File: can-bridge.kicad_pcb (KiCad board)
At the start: 2 copper layers, 59.5 x 54 mm, 14 parts, among them J102 CAN1, SW101 78RB02ST, SW102 Reset, U102 MCP2551-I-SN, U104 TXB0104PW

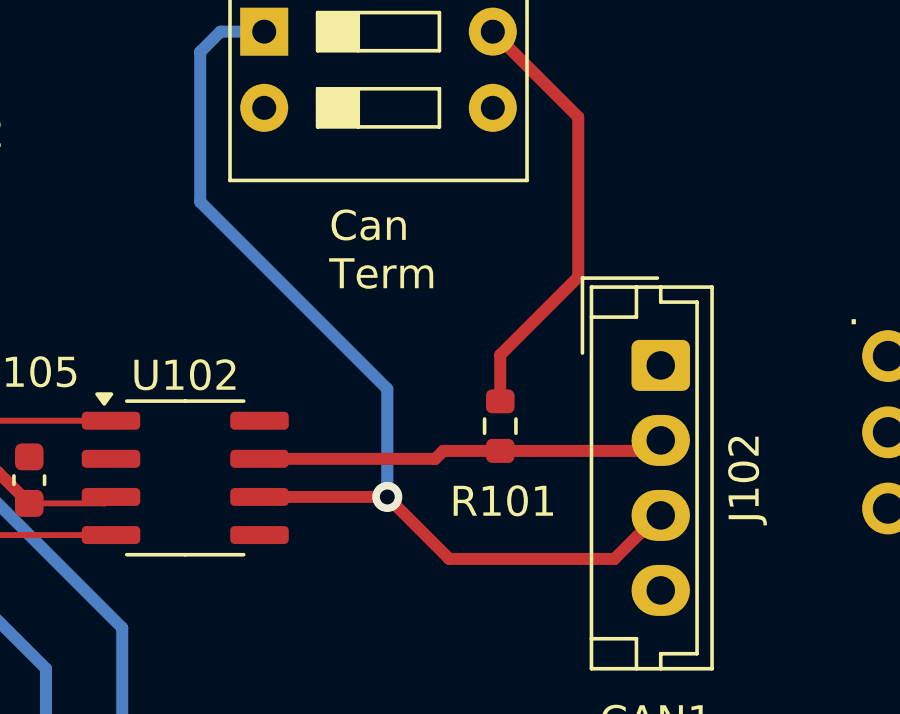
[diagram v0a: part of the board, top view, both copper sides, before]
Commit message: Added README.md and image of prototype
Changed R101 resistor to 1206 footprint
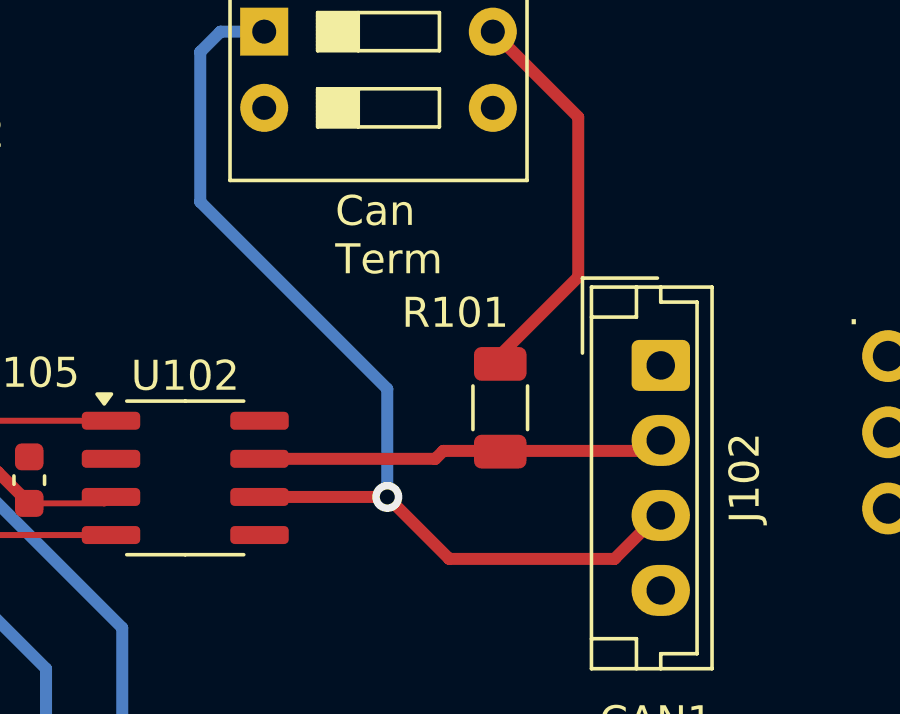
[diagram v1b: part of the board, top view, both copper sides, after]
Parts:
- R101: footprint Resistor_SMD:R_0603_1608Metric -> Resistor_SMD:R_1206_3216Metric
- moved R101 0.61 mm to (162.5, 98.5)
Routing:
- net Net-(R101-Pad1): track 14.6 -> 13.0 mm
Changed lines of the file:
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@@
 		)
 	)
-	(footprint "Resistor_SMD:R_0603_1608Metric"
+	(footprint "Resistor_SMD:R_1206_3216Metric"
 		(layer "F.Cu")
-		(at 162.5 99.075 -90)
-		(descr "Resistor SMD 0603 (1608 Metric), square (rectangular) end terminal, IPC_7351 nominal, (Body size source: IPC-SM-782 page 72, https://www.pcb-3d.com/wordpress/wp-content/uploads/ipc-sm-782a_amendment_1_and_2.pdf), generated with kicad-footprint-generator")
+		(at 162.5 98.4625 -90)
+		(descr "Resistor SMD 1206 (3216 Metric), square (rectangular) end terminal, IPC_7351 nominal, (Body size source: IPC-SM-782 page 72, https://www.pcb-3d.com/wordpress/wp-content/uploads/ipc-sm-782a_amendment_1_and_2.pdf), generated with kicad-footprint-generator")
 		(tags "resistor")
 		(property "Reference" "R101"
-			(at 2.525 -0.1 180)
+			(at -3.1625 1.5 0)
 			(layer "F.SilkS")
 			(effects
@@
 		)
 		(property "Value" "120"
-			(at 0 1.43 90)
+			(at 0 1.82 -90)
 			(layer "F.Fab")
 			(effects
@@
 			)
 		)
-		(property "Footprint" "Resistor_SMD:R_0603_1608Metric"
+		(property "Footprint" "Resistor_SMD:R_1206_3216Metric"
 			(at 0 0 -90)
 			(unlocked yes)
@@
 		(attr smd)
 		(fp_line
-			(start -0.237258 0.5225)
-			(end 0.237258 0.5225)
+			(start -0.727064 0.91)
+			(end 0.727064 0.91)
 			(stroke
 				(width 0.12)
@@
 		)
 		(fp_line
-			(start -0.237258 -0.5225)
-			(end 0.237258 -0.5225)
+			(start -0.727064 -0.91)
+			(end 0.727064 -0.91)
 			(stroke
 				(width 0.12)
@@
 		)
 		(fp_line
-			(start -1.48 0.73)
-			(end -1.48 -0.73)
+			(start -2.28 1.12)
+			(end -2.28 -1.12)
 			(stroke
 				(width 0.05)
@@
 		)
 		(fp_line
-			(start 1.48 0.73)
-			(end -1.48 0.73)
+			(start 2.28 1.12)
+			(end -2.28 1.12)
 			(stroke
 				(width 0.05)
@@
 		)
 		(fp_line
-			(start -1.48 -0.73)
-			(end 1.48 -0.73)
+			(start -2.28 -1.12)
+			(end 2.28 -1.12)
 			(stroke
 				(width 0.05)
@@
 		)
 		(fp_line
-			(start 1.48 -0.73)
-			(end 1.48 0.73)
+			(start 2.28 -1.12)
+			(end 2.28 1.12)
 			(stroke
 				(width 0.05)
@@
 		)
 		(fp_line
-			(start -0.8 0.4125)
-			(end -0.8 -0.4125)
+			(start -1.6 0.8)
+			(end -1.6 -0.8)
 			(stroke
 				(width 0.1)
@@
 		)
 		(fp_line
-			(start 0.8 0.4125)
-			(end -0.8 0.4125)
+			(start 1.6 0.8)
+			(end -1.6 0.8)
 			(stroke
 				(width 0.1)
@@
 		)
 		(fp_line
-			(start -0.8 -0.4125)
-			(end 0.8 -0.4125)
+			(start -1.6 -0.8)
+			(end 1.6 -0.8)
 			(stroke
 				(width 0.1)
@@
 		)
 		(fp_line
-			(start 0.8 -0.4125)
-			(end 0.8 0.4125)
+			(start 1.6 -0.8)
+			(end 1.6 0.8)
 			(stroke
 				(width 0.1)
@@
 		)
 		(fp_text user "${REFERENCE}"
-			(at 0 0 90)
+			(at 0 0 -90)
 			(layer "F.Fab")
 			(effects
 				(font
-					(size 0.4 0.4)
-					(thickness 0.06)
+					(size 0.8 0.8)
+					(thickness 0.12)
 				)
 			)
 		)
 		(pad "1" smd roundrect
-			(at -0.825 0 270)
-			(size 0.8 0.95)
+			(at -1.4625 0 270)
+			(size 1.125 1.75)
 			(layers "F.Cu" "F.Paste" "F.Mask")
-			(roundrect_rratio 0.25)
+			(roundrect_rratio 0.222222)
 			(net 51 "Net-(R101-Pad1)")
 			(pintype "passive")
 		)
 		(pad "2" smd roundrect
-			(at 0.825 0 270)
-			(size 0.8 0.95)
+			(at 1.4625 0 270)
+			(size 1.125 1.75)
 			(layers "F.Cu" "F.Paste" "F.Mask")
-			(roundrect_rratio 0.25)
+			(roundrect_rratio 0.222222)
 			(net 35 "CANH1")
 			(pintype "passive")
 		)
-		(model "${KICAD8_3DMODEL_DIR}/Resistor_SMD.3dshapes/R_0603_1608Metric.wrl"
+		(model "${KICAD8_3DMODEL_DIR}/Resistor_SMD.3dshapes/R_1206_3216Metric.wrl"
 			(offset
 				(xyz 0 0 0)
@@
 	)
 	(gr_text "Can\nTerm"
-		(at 156.8 94.6 0)
+		(at 157 94.1 0)
 		(layer "F.SilkS")
 		(effects
@@
 	)
 	(segment
-		(start 162.5 98.25)
-		(end 162.5 96.7)
-		(width 0.4)
-		(layer "F.Cu")
-		(net 51)
-	)
-	(segment
